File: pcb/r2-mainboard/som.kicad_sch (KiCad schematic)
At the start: 14 parts, among them J21 MICRO_SD(TFC-WPAPR-08), J26 BTH-060-01-L-D-A-K-TR, J27 BTH-060-01-L-D-A-K-TR, X2 PCM-071

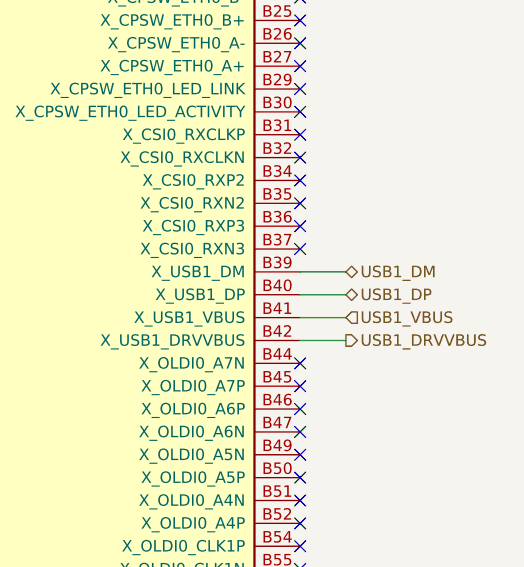
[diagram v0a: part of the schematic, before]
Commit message: Recover from the KiCad crash; finish the USB1_D+/D- rename
KiCad crashed and deleted 150 tracked files plus 19 untracked ones.
Recovery, in the order that matters:

  1. copied _restore_backup_2026-08-31T20-57-08-688 aside (261 MB)
  2. rescued the 4 untracked files that existed only there -- the
     PHYTEC PCM-071 STEP/x_t/Basic models and the library/3dmodels copy.
     The other 15 were __pycache__, .lck and .bak.
  3. git checkout of the 150 deletions (deletions only, so the six
     modified files were never touched)
  4. three files the crash had *rolled back* rather than deleted, and
     which git checkout therefore missed, restored from HEAD:
       r2.kicad_sym    -- was 11 symbols, missing TPS2553DBV,
                          BTH-060_AB/CD and BOM_ITEM, and carrying the
                          superseded PCM-071 symbol: the pre-2026-08-20
                          state, before the SoM was split in two
       sym-lib-table   -- had lost the Reflow declaration
       fp-lib-table    -- had lost Reflow and (version 7)

r2.kicad_pcb was not damaged -- 328 footprints, 471 segments, same as
HEAD. Rescuing PCM-071_1573-1.STEP also repairs X2's 3D model path,
which an earlier restore had broken.

Separately, the USB1 net rename is finished at the owner's request:
som.kicad_sch USB1_DM/DP -> USB1_D-/D+ (the J26 X_USB1_* pin names are
PHYTEC's and are untouched), and a USB1_+ typo on U57's second ESD stub
in io_expansion corrected to USB1_D+. sheet_pins + wire_root re-run:
113 names on 233 sheet pins, 113 joined, 0 one-sided. All five USB1
nets verified node-for-node.

⚠ The tree is mid-renumber (J200/U200/U300... appearing) and carries one
severed net: +3V3_TOUCH reaches only J22.1, while U54.A1 and C517.1 sit
on an unnamed Net-(U54-OUT). Committed as-is so the recovery is not at
risk from another crash; the break is called out rather than hidden.

Co-Authored-By: Claude Opus 5 <noreply@anthropic.com>
Claude-Session: https://claude.ai/code/session_01MHTAe6Znh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
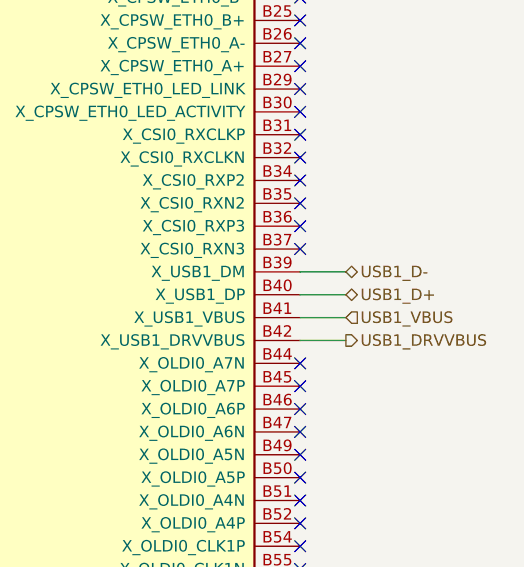
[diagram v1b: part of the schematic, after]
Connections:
- net USB1_DM renamed USB1_D-
- net USB1_DP renamed USB1_D+
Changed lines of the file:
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@@
 		)
 	)
-	(hierarchical_label "USB1_DM"
+	(hierarchical_label "USB1_D-"
 		(shape bidirectional)
 		(at 391.16 64.77 0)
@@
 		)
 	)
-	(hierarchical_label "USB1_DP"
+	(hierarchical_label "USB1_D+"
 		(shape bidirectional)
 		(at 391.16 67.31 0)

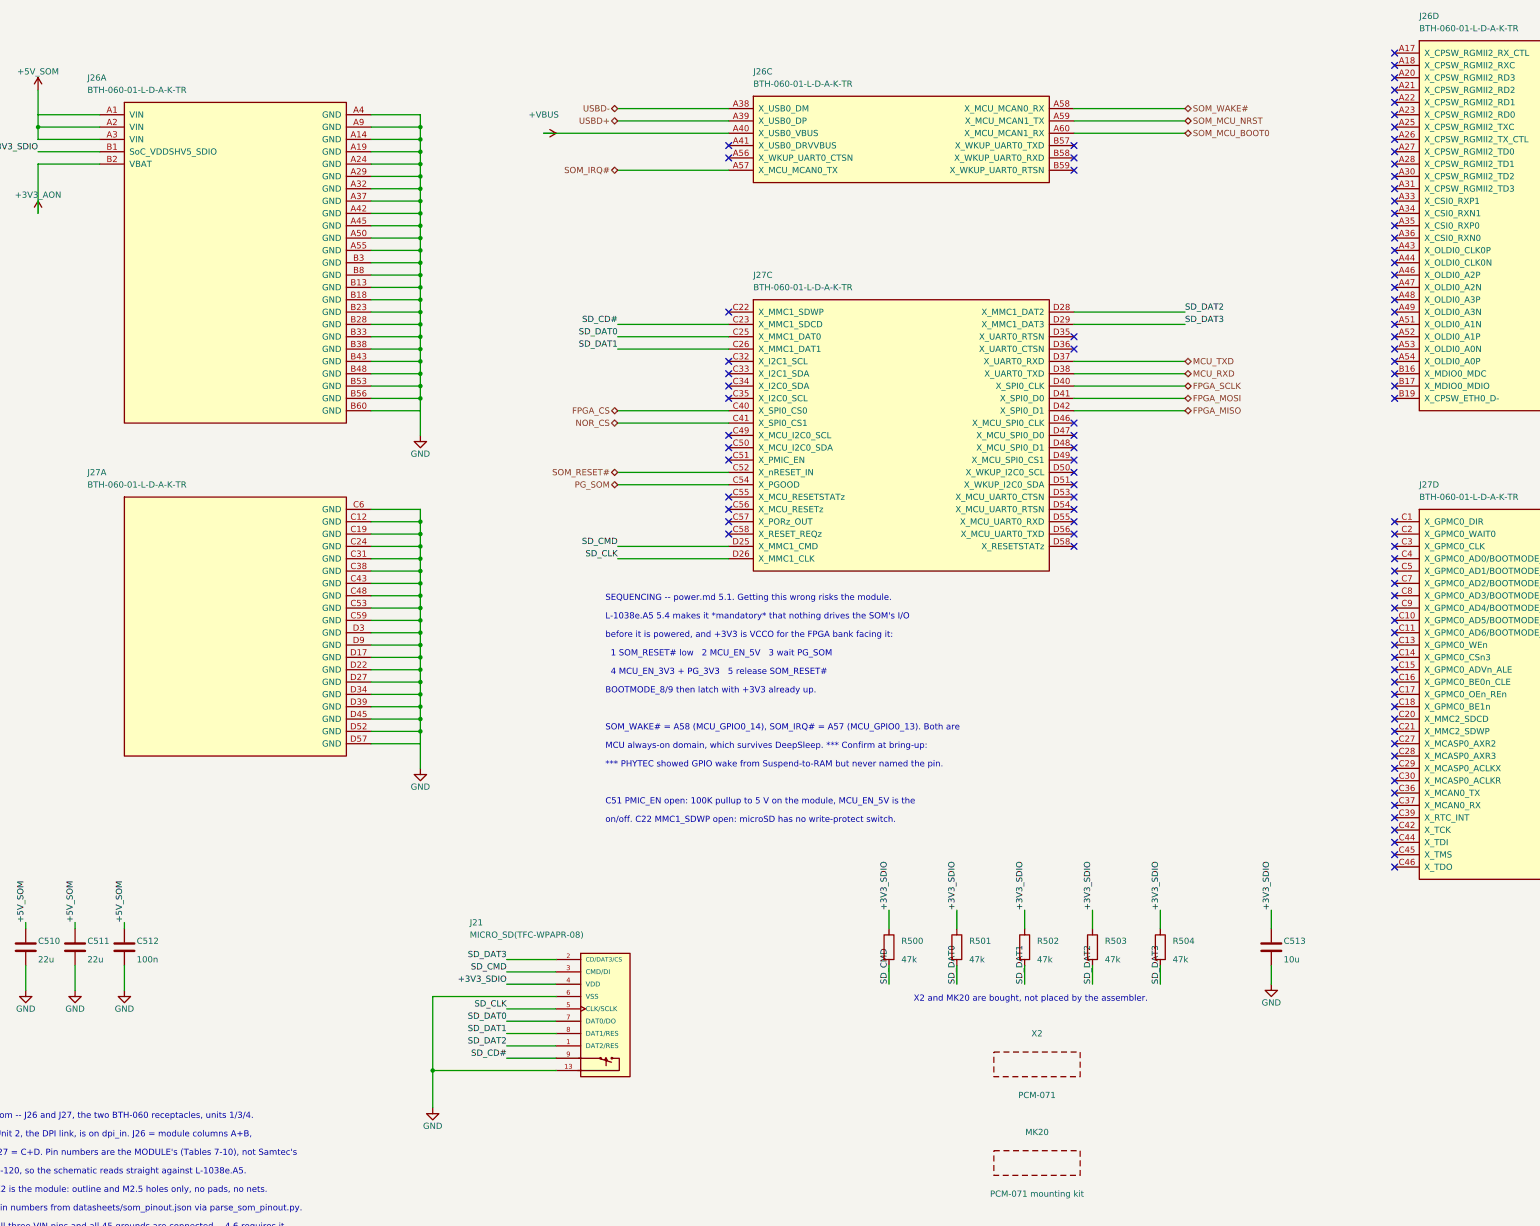
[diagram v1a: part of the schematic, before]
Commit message: R2: renumber every sheet to the page-based designator scheme
The owner's scheme is classifier + sheet page + two-digit part from 00. Four
sheets already used it; this converts the remaining nine, so all thirteen now
agree: pages 2-9 take three digits, pages 10-14 four. 292 of 333 designators
changed. A part shared by several sheets takes its lowest page, so the FPGA is
U700 (pages 7-9) and the two SoM connectors are J501/J502 (pages 5-6).

The whole risk here is silently rewiring the board, so the netlist was diffed
rather than eyeballed:

  nets 519 -> 519, total pin connections 1563 -> 1563
  named nets present in both whose pin multiset changed: 0
  ERC unchanged at 14 errors / 20 warnings
  check_ucf.py: 99 balls matched, 0 failures

That last one matters most: it resolves the gateware's 113 UCF constraints to
board nets *by ball name*, so it is the sharpest detector of the corruption
this change could cause.

Two earlier attempts did cause exactly that. A bare quoted-string substitution
also rewrites FPGA ball names (C1, D2, N11, T1) and BTH-060 pin names (A1-D60),
which are spelled exactly like designators; one run left ERC identical while 40
nets came back with a different pin multiset. The tool now substitutes only at
the two positions that store an instance's designator, and excludes every pin
name everywhere else. docs/layout.md 9.5 records the hazard and how to prove a
renumber was clean.

Only the three scripts that read the design are updated. The gen_*/patch_*/
port_r1.py scripts keep the old names deliberately: each wrote a sheet once and
has not been re-runnable since it was hand-edited in Eeschema, so they are a
historical record -- and port_r1.py's dict keys are R1 designators that were
never renumbered at all.

Co-Authored-By: Claude Opus 5 <noreply@anthropic.com>
Claude-Session: https://claude.ai/code/session_01MHTAe6ZnhogTEgtyPcLhwG
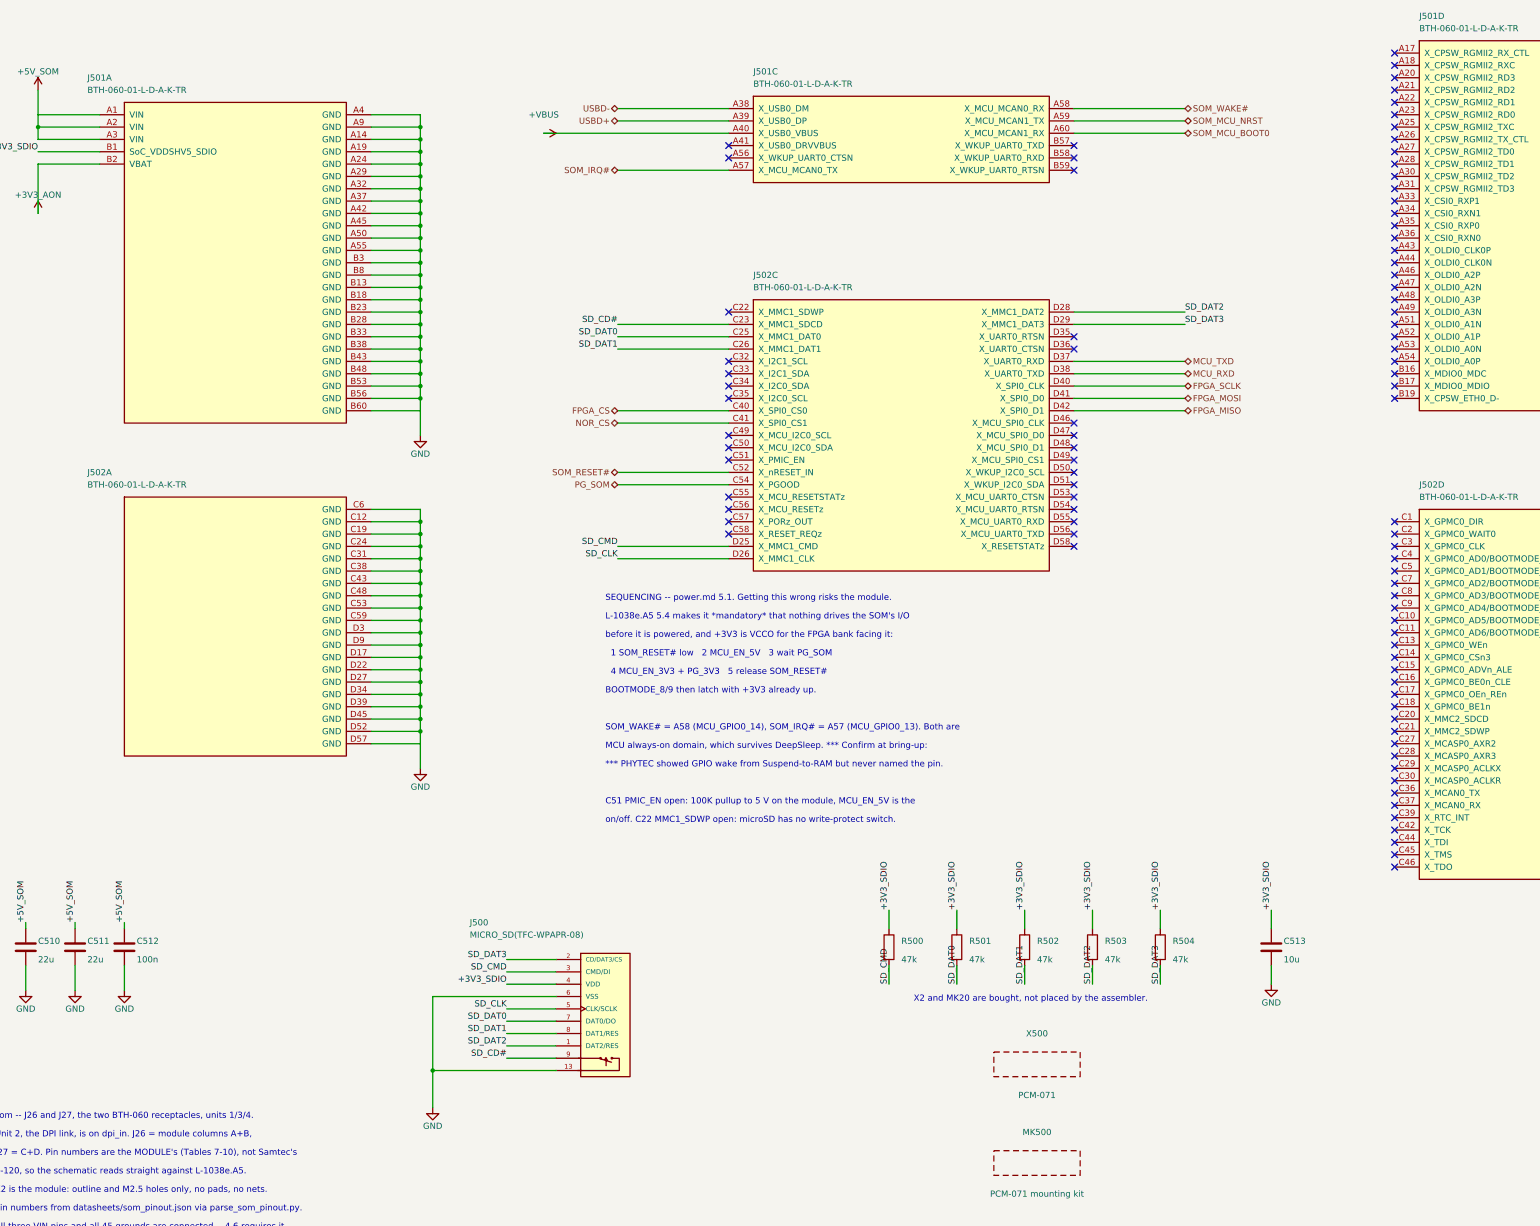
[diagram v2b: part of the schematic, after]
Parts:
- renumbered J21 to J500, J26 to J501, J27 to J502, MK20 to MK500, X2 to X500
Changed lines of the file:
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@@
 		(in_pos_files yes)
 		(dnp no)
-		(property "Reference" "X2"
+		(property "Reference" "X500"
 			(at 241.3 228.6 0)
 			(show_name no)
@@
 			(project "r2"
 				(path "/dee825bf-c2f1-415d-afdf-cf702072a6e8/04dc5b7f-25a0-4938-affb-936b9470a54e"
-					(reference "X2")
+					(reference "X500")
 					(unit 1)
 				)
@@
 		(in_pos_files yes)
 		(dnp no)
-		(property "Reference" "J27"
+		(property "Reference" "J502"
 			(at 320.04 115.57 0)
 			(show_name no)
@@
 			(project "r2"
 				(path "/dee825bf-c2f1-415d-afdf-cf702072a6e8/04dc5b7f-25a0-4938-affb-936b9470a54e"
-					(reference "J27")
+					(reference "J502")
 					(unit 4)
 				)
@@
 		(in_pos_files yes)
 		(dnp no)
-		(property "Reference" "J26"
+		(property "Reference" "J501"
 			(at 320.04 19.05 0)
 			(show_name no)
@@
 			(project "r2"
 				(path "/dee825bf-c2f1-415d-afdf-cf702072a6e8/04dc5b7f-25a0-4938-affb-936b9470a54e"
-					(reference "J26")
+					(reference "J501")
 					(unit 4)
 				)
@@
 		(in_pos_files yes)
 		(dnp no)
-		(property "Reference" "J27"
+		(property "Reference" "J502"
 			(at 182.88 72.39 0)
 			(show_name no)
@@
 			(project "r2"
 				(path "/dee825bf-c2f1-415d-afdf-cf702072a6e8/04dc5b7f-25a0-4938-affb-936b9470a54e"
-					(reference "J27")
+					(reference "J502")
 					(unit 3)
 				)
@@
 		(in_pos_files yes)
 		(dnp no)
-		(property "Reference" "J26"
+		(property "Reference" "J501"
 			(at 182.88 30.48 0)
 			(show_name no)
@@
 			(project "r2"
 				(path "/dee825bf-c2f1-415d-afdf-cf702072a6e8/04dc5b7f-25a0-4938-affb-936b9470a54e"
-					(reference "J26")
+					(reference "J501")
 					(unit 3)
 				)
@@
 		(in_pos_files yes)
 		(dnp no)
-		(property "Reference" "MK20"
+		(property "Reference" "MK500"
 			(at 241.3 248.92 0)
 			(show_name no)
@@
 			(project "r2"
 				(path "/dee825bf-c2f1-415d-afdf-cf702072a6e8/04dc5b7f-25a0-4938-affb-936b9470a54e"
-					(reference "MK20")
+					(reference "MK500")
 					(unit 1)
 				)
@@
 		(in_pos_files yes)
 		(dnp no)
-		(property "Reference" "J21"
+		(property "Reference" "J500"
 			(at 124.46 205.74 0)
 			(show_name no)
@@
 			(project "r2"
 				(path "/dee825bf-c2f1-415d-afdf-cf702072a6e8/04dc5b7f-25a0-4938-affb-936b9470a54e"
-					(reference "J21")
+					(reference "J500")
 					(unit 1)
 				)
@@
 		(in_pos_files yes)
 		(dnp no)
-		(property "Reference" "J27"
+		(property "Reference" "J502"
 			(at 45.72 113.03 0)
 			(show_name no)
@@
 			(project "r2"
 				(path "/dee825bf-c2f1-415d-afdf-cf702072a6e8/04dc5b7f-25a0-4938-affb-936b9470a54e"
-					(reference "J27")
+					(reference "J502")
 					(unit 1)
 				)
@@
 		(in_pos_files yes)
 		(dnp no)
-		(property "Reference" "J26"
+		(property "Reference" "J501"
 			(at 45.72 31.75 0)
 			(show_name no)
@@
 			(project "r2"
 				(path "/dee825bf-c2f1-415d-afdf-cf702072a6e8/04dc5b7f-25a0-4938-affb-936b9470a54e"
-					(reference "J26")
+					(reference "J501")
 					(unit 1)
 				)
